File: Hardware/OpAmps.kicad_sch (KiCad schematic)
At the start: 67 parts, among them J7 Audio_Breakout, J8 Gate_Breakout, U10 TL074, U11 TL074, U12 TL074, U13 TL074, U14 TL074, U15 TL074

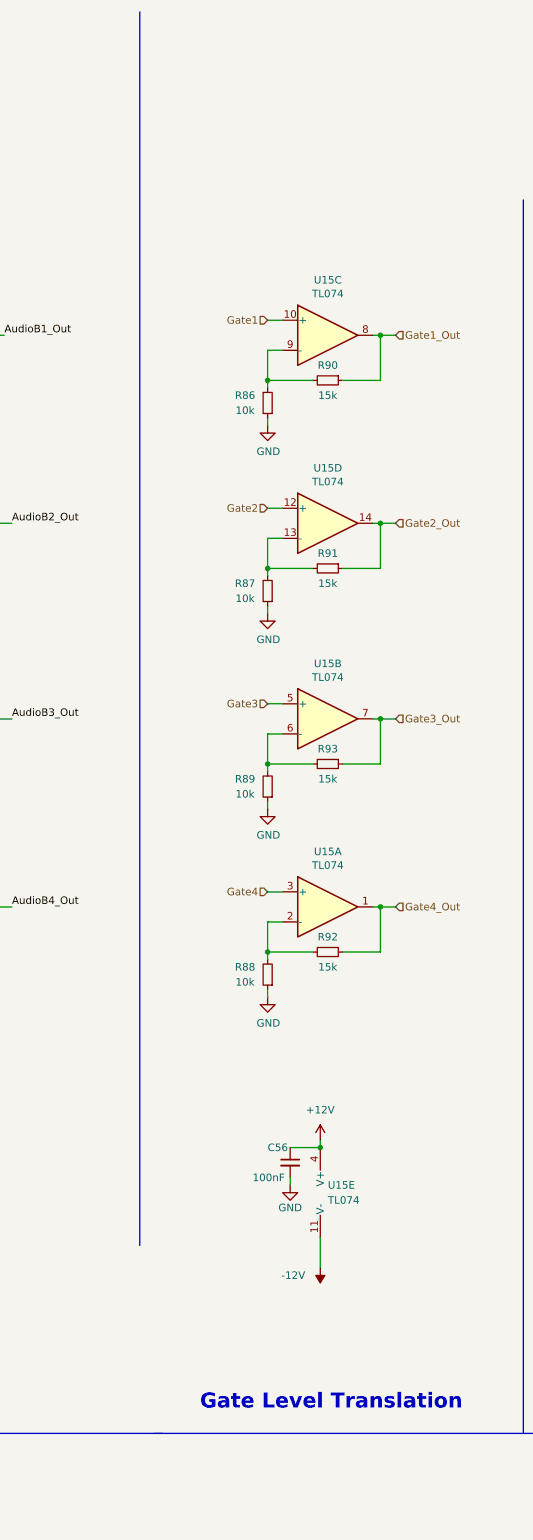
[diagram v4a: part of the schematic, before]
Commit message: Gate mechanism working
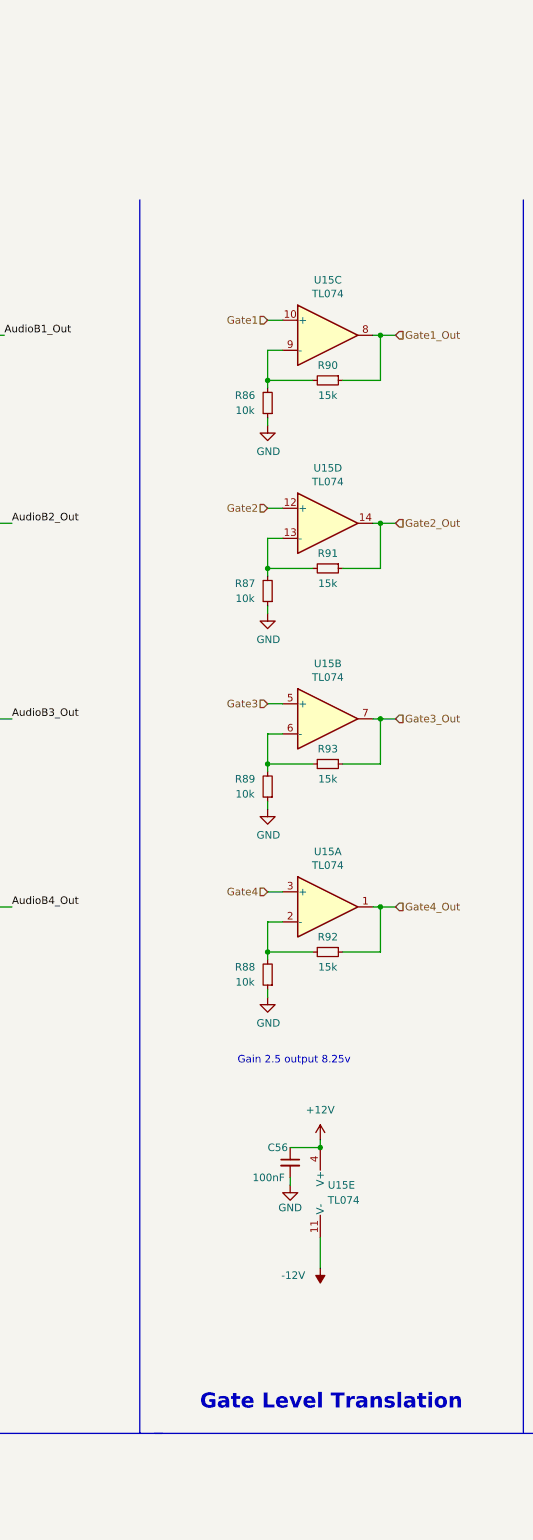
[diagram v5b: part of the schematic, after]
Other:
- note added: "Gain 2.5 output 8.25v"
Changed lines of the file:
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@@
     (stroke (width 0) (type default) (color 0 0 0 0))
   )
-  (polyline (pts (xy 256.54 -19.05) (xy 256.54 189.23))
+  (polyline (pts (xy 256.54 12.7) (xy 256.54 220.98))
     (stroke (width 0) (type default) (color 0 0 0 0))
   )
@@
     (effects (font (size 2.54 2.54) (thickness 0.508) bold) (justify left bottom))
   )
+  (text "Gain 2.5 output 8.25v" (at 273.05 158.75 0)
+    (effects (font (size 1.27 1.27)) (justify left bottom))
+  )
   (label "AudioA1_Out" (at 341.63 26.67 180)

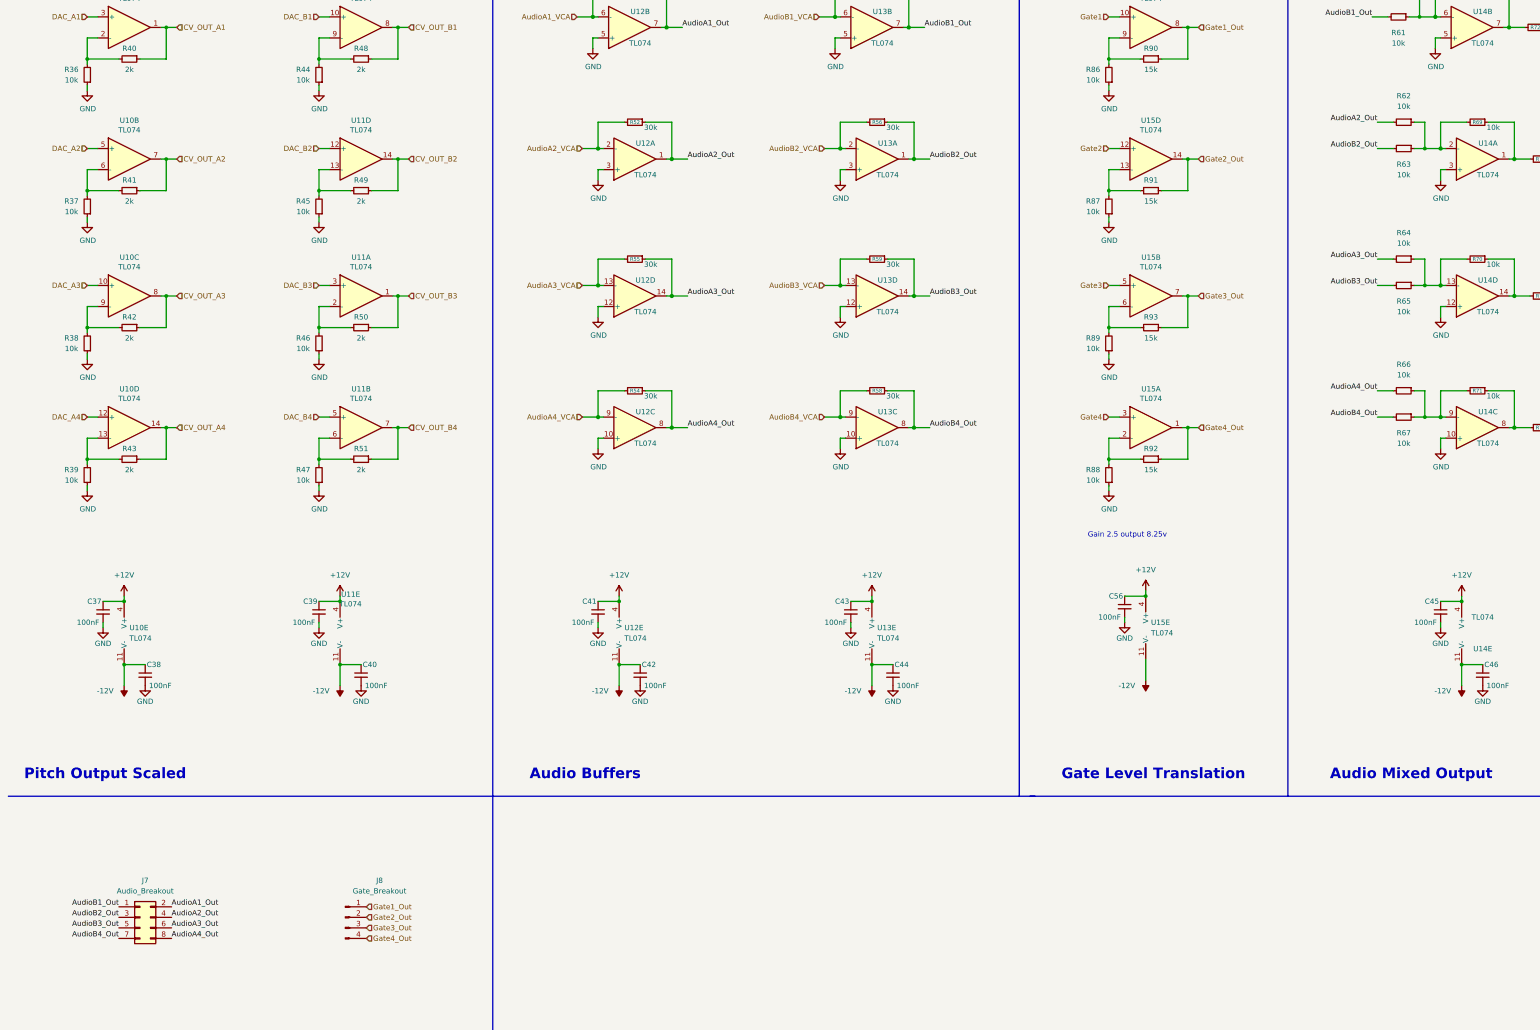
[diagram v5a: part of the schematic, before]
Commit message: Increased CV output range from 6v - 7.13v to increase maximum output octave
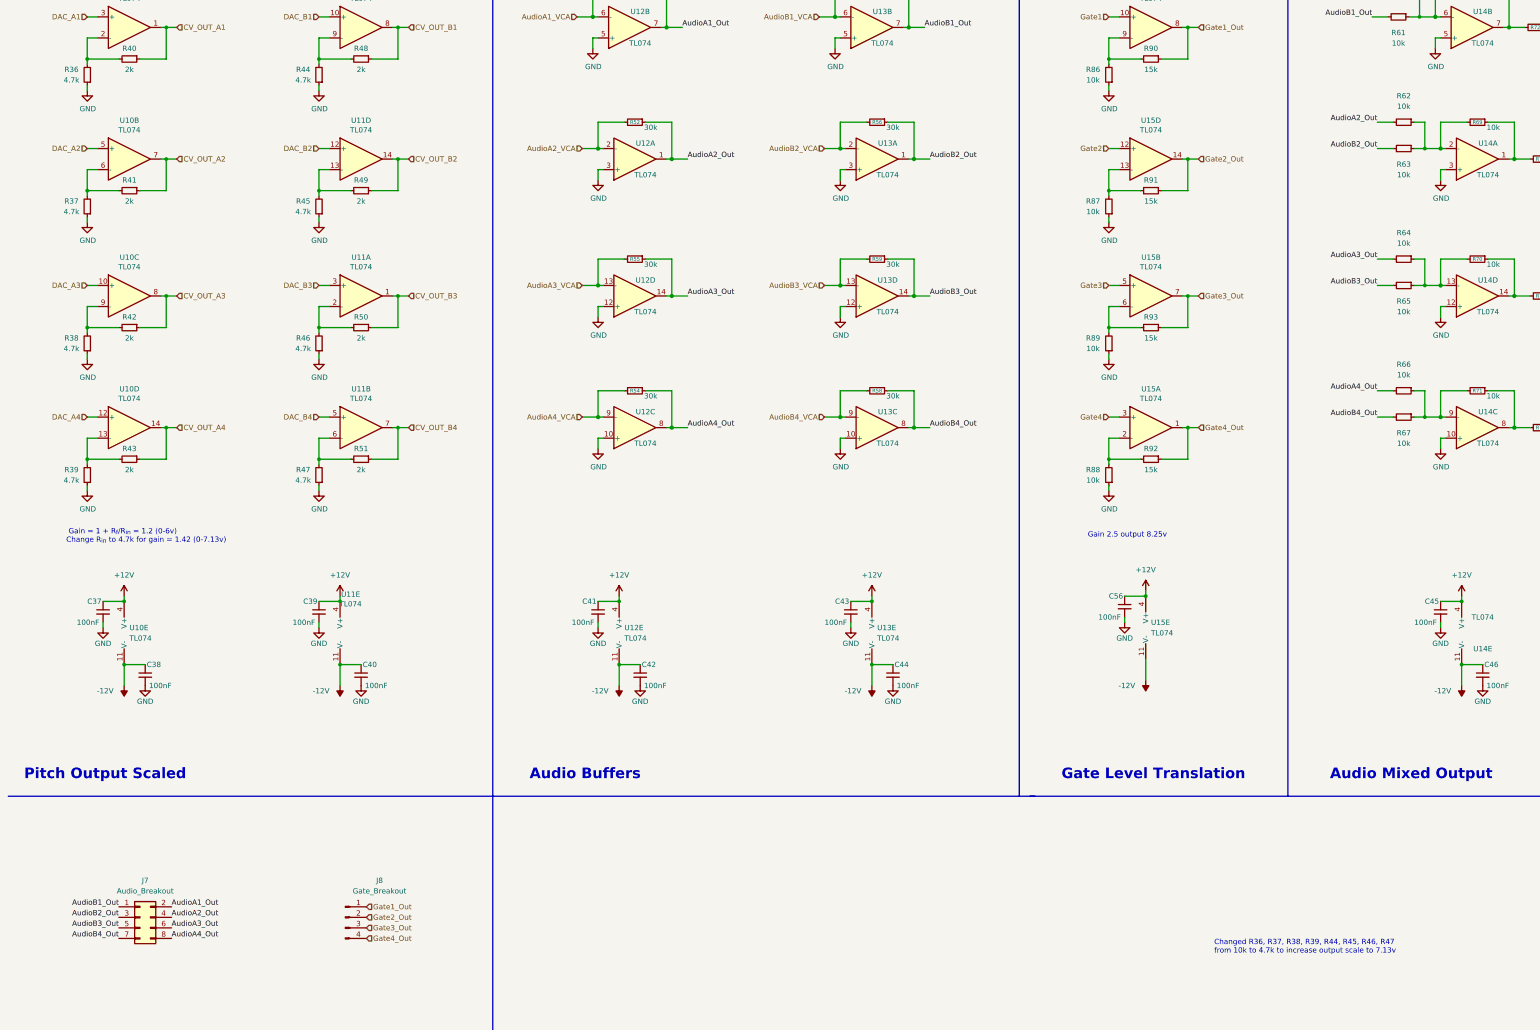
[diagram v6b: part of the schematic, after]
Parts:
- R36, R37, R38, R39, R44, R45, R46, R47: value 10k -> 4.7k
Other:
- note added: "Changed R36, R37, R38, R39, R44, R45, R46, R47 from 10k to 4.7k to increase output scale to 7.13v"
- note added: "Gain = 1 + R_{f}/R_{in} = 1.2 (0-6v) Change R_{in} to 4.7k for gain = 1.42 (0-7.13v)"
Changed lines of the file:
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@@
+    (effects (font (size 1.27 1.27)) (justify left bottom))
+  )
+  (text " Gain = 1 + R_{f}/R_{in} = 1.2 (0-6v)\nChange R_{in} to 4.7k for gain = 1.42 (0-7.13v)"
+    (at 26.67 160.02 0)
+    (effects (font (size 1.27 1.27)) (justify left bottom))
+  )
+  (text "Changed R36, R37, R38, R39, R44, R45, R46, R47 \nfrom 10k to 4.7k to increase output scale to 7.13v"
+    (at 303.53 259.08 0)
     (effects (font (size 1.27 1.27)) (justify left bottom))
   )
@@
     (in_bom yes) (on_board yes)
     (property "Reference" "R37" (id 0) (at 27.94 77.47 0))
-    (property "Value" "10k" (id 1) (at 27.94 80.01 0))
+    (property "Value" "4.7k" (id 1) (at 27.94 80.01 0))
     (property "Footprint" "Resistor_SMD:R_0603_1608Metric" (id 2) (at 31.75 78.74 0)
       (effects (font (size 1.27 1.27)) hide)
@@
     (in_bom yes) (on_board yes)
     (property "Reference" "R46" (id 0) (at 83.82 110.49 0))
-    (property "Value" "10k" (id 1) (at 83.82 113.03 0))
+    (property "Value" "4.7k" (id 1) (at 83.82 113.03 0))
     (property "Footprint" "Resistor_SMD:R_0603_1608Metric" (id 2) (at 87.63 111.76 0)
       (effects (font (size 1.27 1.27)) hide)
@@
     (in_bom yes) (on_board yes)
     (property "Reference" "R38" (id 0) (at 27.94 110.49 0))
-    (property "Value" "10k" (id 1) (at 27.94 113.03 0))
+    (property "Value" "4.7k" (id 1) (at 27.94 113.03 0))
     (property "Footprint" "Resistor_SMD:R_0603_1608Metric" (id 2) (at 31.75 111.76 0)
       (effects (font (size 1.27 1.27)) hide)
@@
     (in_bom yes) (on_board yes)
     (property "Reference" "R39" (id 0) (at 27.94 142.24 0))
-    (property "Value" "10k" (id 1) (at 27.94 144.78 0))
+    (property "Value" "4.7k" (id 1) (at 27.94 144.78 0))
     (property "Footprint" "Resistor_SMD:R_0603_1608Metric" (id 2) (at 31.75 143.51 0)
       (effects (font (size 1.27 1.27)) hide)
@@
     (in_bom yes) (on_board yes)
     (property "Reference" "R36" (id 0) (at 27.94 45.72 0))
-    (property "Value" "10k" (id 1) (at 27.94 48.26 0))
+    (property "Value" "4.7k" (id 1) (at 27.94 48.26 0))
     (property "Footprint" "Resistor_SMD:R_0603_1608Metric" (id 2) (at 31.75 46.99 0)
       (effects (font (size 1.27 1.27)) hide)
@@
     (in_bom yes) (on_board yes)
     (property "Reference" "R44" (id 0) (at 83.82 45.72 0))
-    (property "Value" "10k" (id 1) (at 83.82 48.26 0))
+    (property "Value" "4.7k" (id 1) (at 83.82 48.26 0))
     (property "Footprint" "Resistor_SMD:R_0603_1608Metric" (id 2) (at 87.63 46.99 0)
       (effects (font (size 1.27 1.27)) hide)
@@
     (in_bom yes) (on_board yes)
     (property "Reference" "R47" (id 0) (at 83.82 142.24 0))
-    (property "Value" "10k" (id 1) (at 83.82 144.78 0))
+    (property "Value" "4.7k" (id 1) (at 83.82 144.78 0))
     (property "Footprint" "Resistor_SMD:R_0603_1608Metric" (id 2) (at 87.63 143.51 0)
       (effects (font (size 1.27 1.27)) hide)
@@
     (in_bom yes) (on_board yes)
     (property "Reference" "R45" (id 0) (at 83.82 77.47 0))
-    (property "Value" "10k" (id 1) (at 83.82 80.01 0))
+    (property "Value" "4.7k" (id 1) (at 83.82 80.01 0))
     (property "Footprint" "Resistor_SMD:R_0603_1608Metric" (id 2) (at 87.63 78.74 0)
       (effects (font (size 1.27 1.27)) hide)

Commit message: Panel version 3
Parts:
- R72, R73, R74, R75: value 1k -> 100
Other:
- note added: "- Changed R36, R37, R38, R39, R44, R45, R46, R47 from 10k to 4.7k to increase output scale to 7.13v - REduce output protection resistors from 1k to 100"
- note removed: "Changed R36, R37, R38, R39, R44, R45, R46, R47 from 10k to 4.7k to increase output scale to 7.13v"

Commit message: Updated component schematic/pcb to v2
Kicad 8.0
Fixing opamp U14 power reversal
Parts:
- J8: symbol Connector:Conn_01x04_Male -> Connector:Conn_01x04_Pin
